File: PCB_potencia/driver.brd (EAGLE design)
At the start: 160 x 100 mm, 38 parts, among them Q1 IRF530, Q2 IRF530, Q3 IRF530, T1 BC547, T2 BC547, T3 2SC1815, T4 2SC1815, T5 BC547, T6 BC547, T7 BC547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

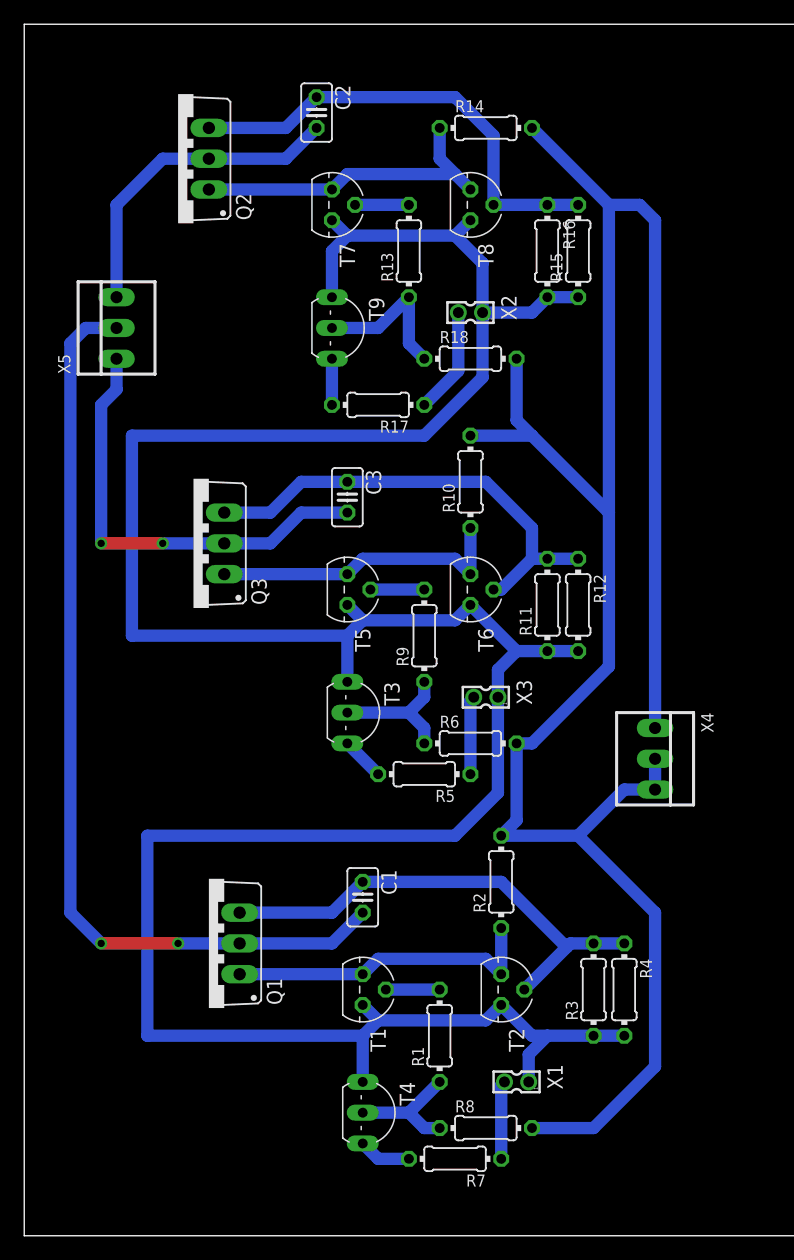
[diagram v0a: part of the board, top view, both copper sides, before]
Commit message: Se corrige transistor para invertir la señal de cada PWM y se ajustan resistencias de potencia
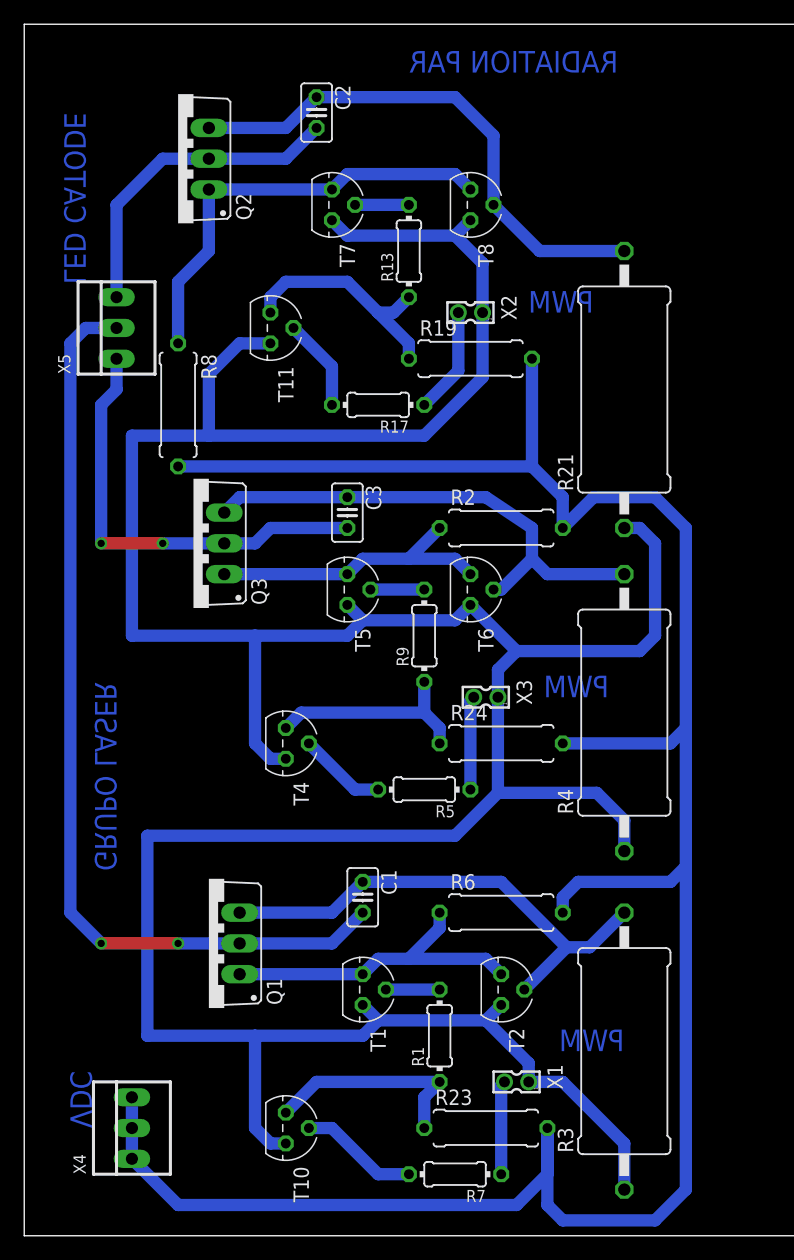
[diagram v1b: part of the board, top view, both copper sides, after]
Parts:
- removed R10, R11, R12, R14, R15, R16: (no value), eagle-ltspice:0204/7
- removed R18: (no value), rcl:0204/7
- removed T3, T9: 2SC1815, transistor:TO92-ECB
- added R19, R23, R24: (no value), resistor:0309/10
- added R21: (no value), resistor:P0817/22
- added T10, T11: BC337, transistor:TO92
- R2: device eagle-ltspice:0204/7 -> resistor:0309/10
- R3, R4: device eagle-ltspice:0204/7 -> resistor:P0817/22
- R6, R8: device rcl:0204/7 -> resistor:0309/10
- T4: value 2SC1815 -> BC337; device transistor:TO92-ECB -> transistor:TO92
- moved R8 64.9 mm to (12.7, 68.6), turned to 270 degrees
- moved X4 52.9 mm to (8.89, 8.89), turned to 90 degrees
- moved T4 31.1 mm to (21.6, 40.6)
- moved R2 29.2 mm to (39.4, 58.4), turned to 0 degrees
- moved R4 22.9 mm to (49.5, 43.2), turned to 90 degrees
- moved R6 14.2 mm to (39.4, 26.7)
- moved R3 5.68 mm to (49.5, 15.2)
- moved C3 1.27 mm to (26.7, 59.7)
- moved R5 1.27 mm to (33.0, 36.8)
- moved R7 1.27 mm to (35.6, 5.08)
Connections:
- net GND: now also R21.1, R4.1, T10.1, T11.1, T4.1; no longer R11.1, R12.2, R15.1, R16.2, R4.2, T3.E, T4.E, T9.E
- net N$13: now also R2.1; no longer R10.1
- net N$15: now also R4.2; no longer R11.2, R12.1
- net N$16: now also R8.1; no longer R14.1
- net N$18: now also R21.2; no longer R15.2, R16.1
- net N$19: now also T11.2; no longer T9.B
- net N$2: now also R6.1; no longer R2.1
- net N$20: now also R19.1, T11.3; no longer R18.1, T9.C
- net N$4: now also T4.2; no longer T3.B
- net N$5: no longer R4.1
- net N$6: now also T10.2; no longer T4.B
- net N$7: now also R24.1, T4.3; no longer R6.1, T3.C
- net N$9: now also R23.1, T10.3; no longer R8.1, T4.C
- net VCC: now also R19.2, R23.2, R24.2; no longer R10.2, R14.2, R18.2
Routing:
- net GND: track 242.4 -> 290.8 mm
- net VCC: track 183.4 -> 199.4 mm
- net N$16: track 27.0 -> 36.4 mm
- net N$9: track 10.5 -> 18.1 mm
- net N$20: track 13.0 -> 19.7 mm
- net N$7: track 11.2 -> 17.6 mm
- net N$6: track 4.34 -> 9.83 mm
- net N$18: track 38.6 -> 44.0 mm
- net N$19: track 3.81 -> 7.67 mm
- net N$4: track 3.59 -> 7.29 mm
- net N$15: track 38.6 -> 41.6 mm
- net N$8: track 6.46 -> 7.73 mm
- net N$10: track 6.46 -> 7.73 mm
- net N$2: track 26.5 -> 27.5 mm
- net N$5: track 40.1 -> 41.2 mm
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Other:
- board text added: "GRUPO LASER"
- board text added: "LED CATODE"
- board text added: "PWM"
- board text added: "RADIATION PAR"
- board text added: "VDC"
